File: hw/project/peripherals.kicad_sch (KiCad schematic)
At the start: 72 parts, among them J1 Battery, J10 I2C, J11 Voltage Monitor, J12 Misc, J2 Phases, J3 FTSH-107-01-L-DV-K-A, J4 Throttle, J5 Hall, J6 Serial, J7 SPI, J8 2.54 Comm, J9 CAN, SW3 USER, U3 ATA6561-GAQW-N

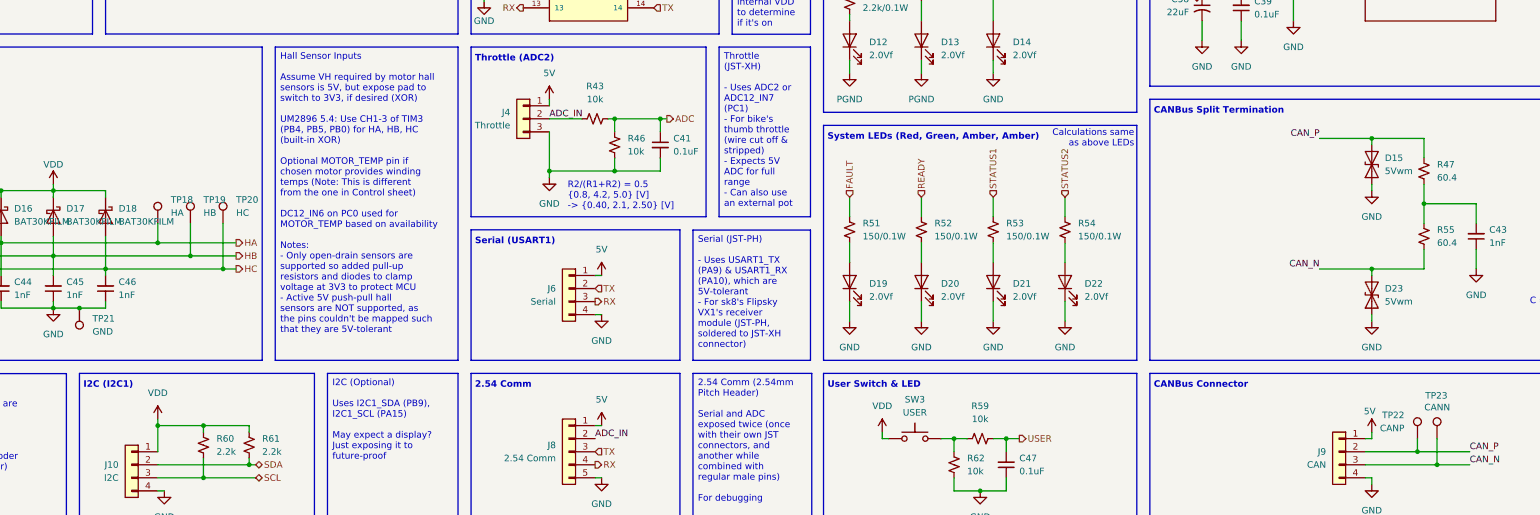
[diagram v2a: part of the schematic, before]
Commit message: Place next tier of components after critical ones
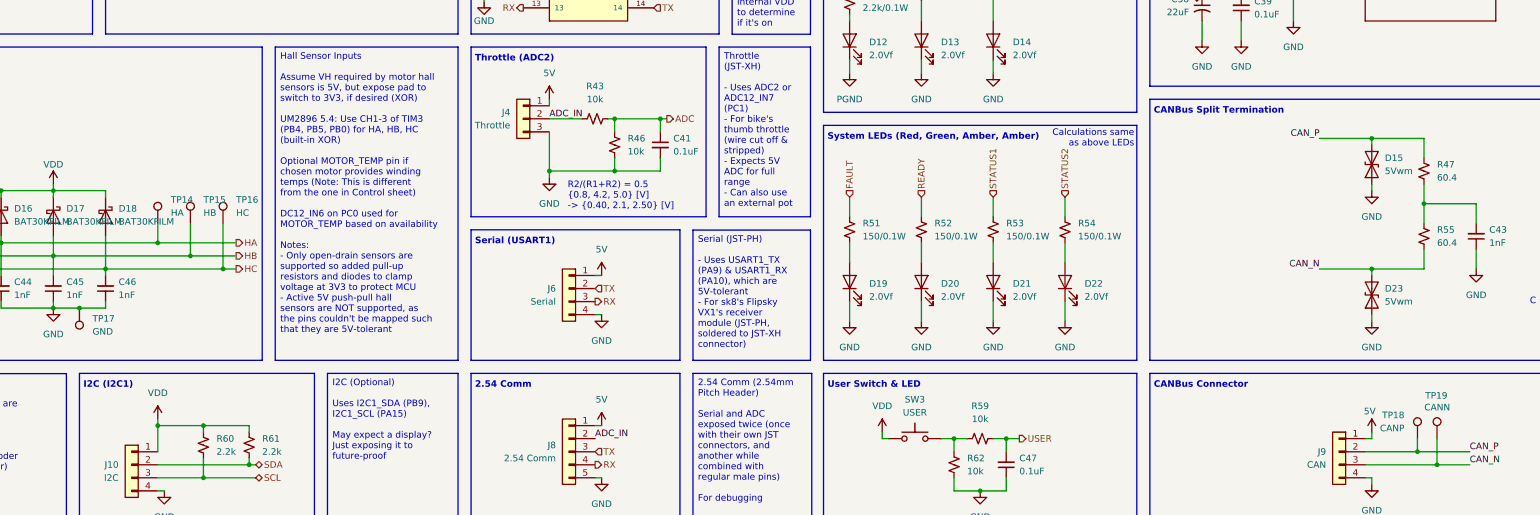
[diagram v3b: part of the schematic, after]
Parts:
- D12, D13, D14, D19, D20, D21, D22: footprint LED_SMD:LED_0603_1608Metric_Pad1.05x0.95mm_HandSolder -> LED_SMD:LED_0603_1608Metric
- R38, R40, R41, R51, R52, R53, R54: footprint Resistor_SMD:R_0603_1608Metric_Pad0.98x0.95mm_HandSolder -> Resistor_SMD:R_0603_1608Metric
- renumbered TP18 to TP14, TP19 to TP15, TP20 to TP16, TP21 to TP17, TP22 to TP18, TP23 to TP19
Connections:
- net GND: now also D13.1 (K)
- net PGND: no longer D13.1 (K)

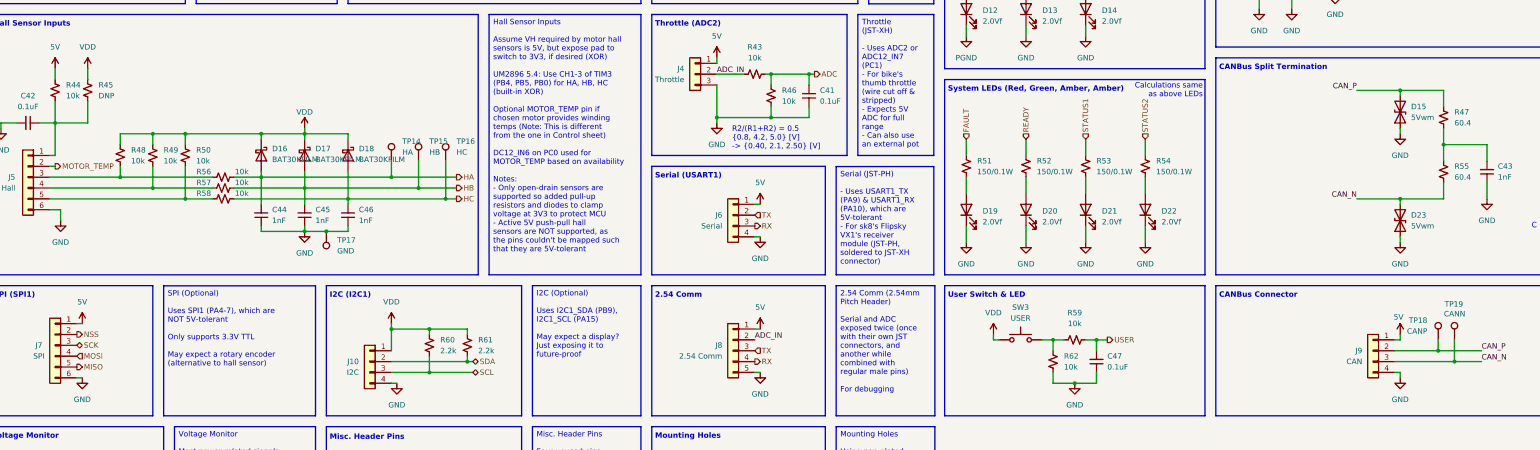
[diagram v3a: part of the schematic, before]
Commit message: Finish laying out all clusters
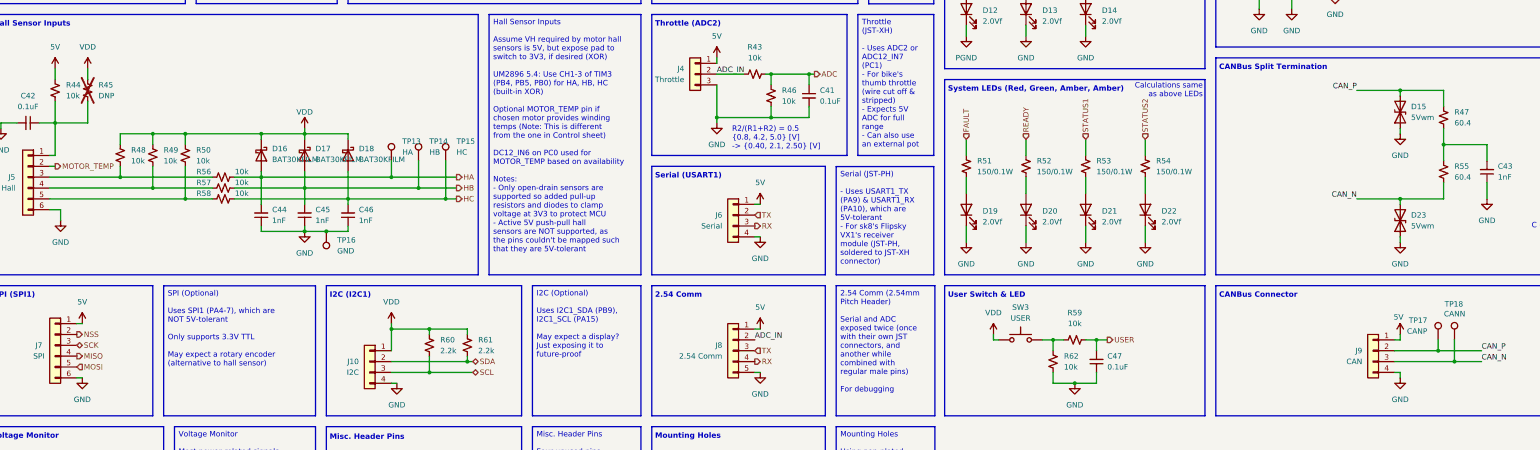
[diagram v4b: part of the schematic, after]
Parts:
- R45: now not fitted
- renumbered TP14 to TP13, TP15 to TP14, TP16 to TP15, TP17 to TP16, TP18 to TP17, TP19 to TP18
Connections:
- net MISO: now also J7.4 (Pin_4); no longer J7.5 (Pin_5)
- net MOSI: now also J7.5 (Pin_5); no longer J7.4 (Pin_4)
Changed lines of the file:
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@@
 	(hierarchical_label "MISO"
 		(shape output)
-		(at 35.56 133.35 0)
+		(at 35.56 130.81 0)
 		(effects
 			(font
@@
 	(hierarchical_label "MOSI"
 		(shape input)
-		(at 35.56 130.81 0)
+		(at 35.56 133.35 0)
 		(effects
 			(font
@@
 		(dnp no)
 		(fields_autoplaced yes)
-		(property "Reference" "#PWR0105"
+		(property "Reference" "#PWR070"
 			(at 257.81 62.23 0)
 			(hide yes)
@@
 			(project "esc"
 				(path "/86a17c4d-db96-42a1-af84-d43fe593f4e6/84ea8536-46c8-4cae-8743-a6718dee2882"
-					(reference "#PWR0105")
+					(reference "#PWR070")
 					(unit 1)
 				)
@@
 		(on_board yes)
 		(in_pos_files yes)
-		(dnp no)
+		(dnp yes)
 		(fields_autoplaced yes)
 		(property "Reference" "R45"
@@
 		(dnp no)
 		(fields_autoplaced yes)
-		(property "Reference" "TP14"
+		(property "Reference" "TP13"
 			(at 111.76 80.5179 0)
 			(show_name no)
@@
 			(project "esc"
 				(path "/86a17c4d-db96-42a1-af84-d43fe593f4e6/84ea8536-46c8-4cae-8743-a6718dee2882"
-					(reference "TP14")
+					(reference "TP13")
 					(unit 1)
 				)
@@
 		(dnp no)
 		(fields_autoplaced yes)
-		(property "Reference" "TP16"
+		(property "Reference" "TP15"
 			(at 124.46 80.5179 0)
 			(show_name no)
@@
 			(project "esc"
 				(path "/86a17c4d-db96-42a1-af84-d43fe593f4e6/84ea8536-46c8-4cae-8743-a6718dee2882"
-					(reference "TP16")
+					(reference "TP15")
 					(unit 1)
 				)
@@
 		(in_pos_files yes)
 		(dnp no)
-		(property "Reference" "TP19"
+		(property "Reference" "TP18"
 			(at 360.172 118.618 0)
 			(show_name no)
@@
 			(project "esc"
 				(path "/86a17c4d-db96-42a1-af84-d43fe593f4e6/84ea8536-46c8-4cae-8743-a6718dee2882"
-					(reference "TP19")
+					(reference "TP18")
 					(unit 1)
 				)
@@
 		(dnp no)
 		(fields_autoplaced yes)
-		(property "Reference" "TP18"
+		(property "Reference" "TP17"
 			(at 351.79 122.4279 0)
 			(show_name no)
@@
 			(project "esc"
 				(path "/86a17c4d-db96-42a1-af84-d43fe593f4e6/84ea8536-46c8-4cae-8743-a6718dee2882"
-					(reference "TP18")
+					(reference "TP17")
 					(unit 1)
 				)
@@
 		(dnp no)
 		(fields_autoplaced yes)
-		(property "Reference" "TP17"
+		(property "Reference" "TP16"
 			(at 96.52 103.6319 0)
 			(show_name no)
@@
 			(project "esc"
 				(path "/86a17c4d-db96-42a1-af84-d43fe593f4e6/84ea8536-46c8-4cae-8743-a6718dee2882"
-					(reference "TP17")
+					(reference "TP16")
 					(unit 1)
 				)
@@
 		(dnp no)
 		(fields_autoplaced yes)
-		(property "Reference" "TP15"
+		(property "Reference" "TP14"
 			(at 118.11 80.5179 0)
 			(show_name no)
@@
 			(project "esc"
 				(path "/86a17c4d-db96-42a1-af84-d43fe593f4e6/84ea8536-46c8-4cae-8743-a6718dee2882"
-					(reference "TP15")
+					(reference "TP14")
 					(unit 1)
 				)

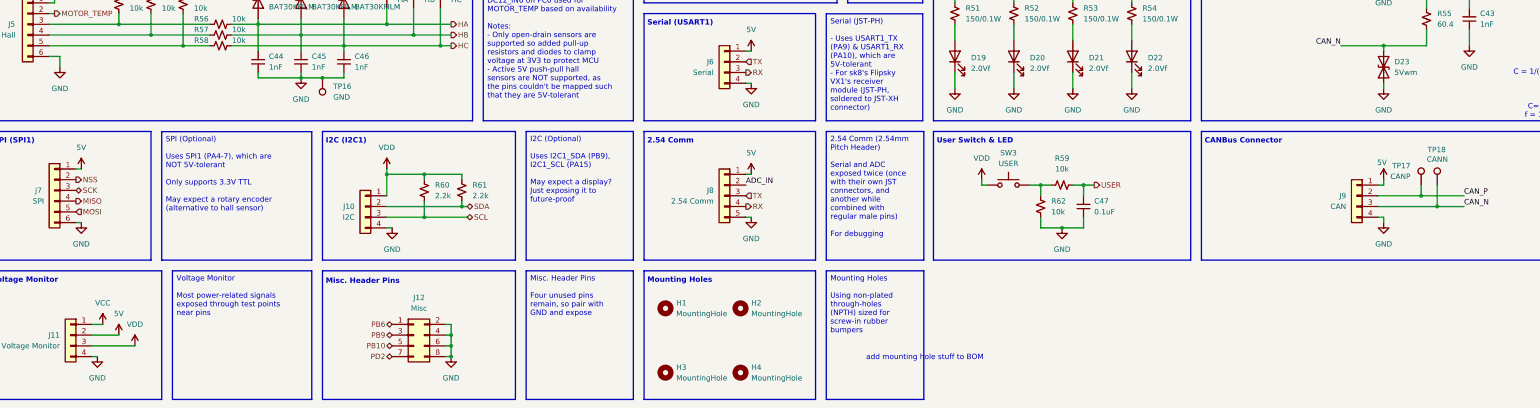
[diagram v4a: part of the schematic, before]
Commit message: Finish most of the layout, just the power stuff next!
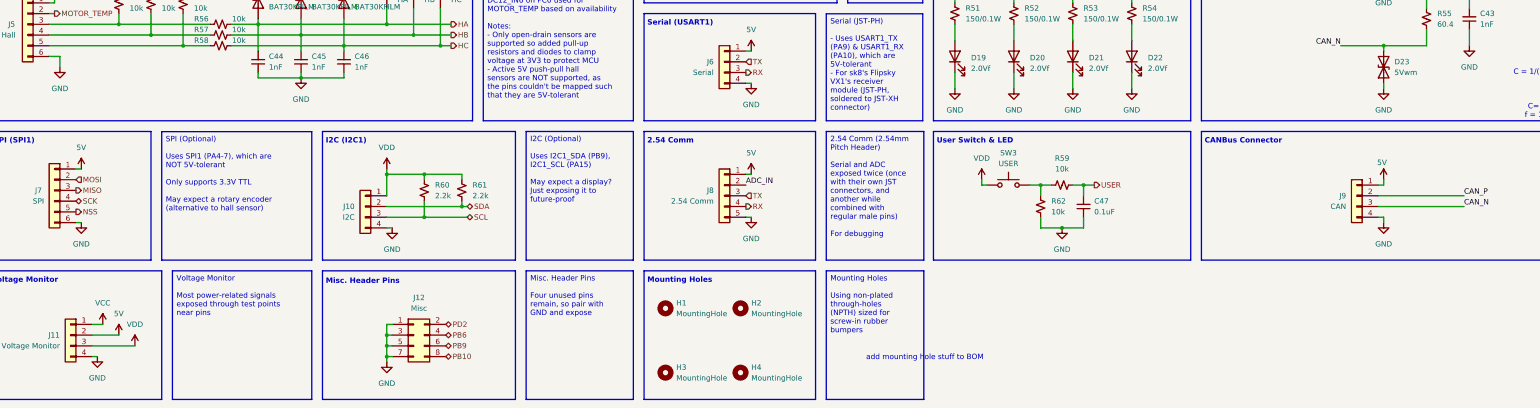
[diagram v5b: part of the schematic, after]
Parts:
- removed TP16: GND, TestPoint:TestPoint_Pad_1.0x1.0mm, symbol Connector:TestPoint
- removed TP17: CANP, TestPoint:TestPoint_Pad_D1.0mm, symbol Connector:TestPoint
- removed TP18: CANN, TestPoint:TestPoint_Pad_D1.0mm, symbol Connector:TestPoint
- J8: footprint Connector_PinSocket_2.54mm:PinSocket_1x05_P2.54mm_Vertical -> Connector_PinHeader_2.54mm:PinHeader_1x05_P2.54mm_Vertical
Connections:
- net GND: now also J12.1 (Pin_1), J12.3 (Pin_3), J12.5 (Pin_5), J12.7 (Pin_7); no longer J12.2 (Pin_2), J12.4 (Pin_4), J12.6 (Pin_6), J12.8 (Pin_8)
- net MISO: now also J7.3 (Pin_3); no longer J7.4 (Pin_4)
- net MOSI: now also J7.2 (Pin_2); no longer J7.5 (Pin_5)
- net NSS: now also J7.5 (Pin_5); no longer J7.2 (Pin_2)
- net PB10: now also J12.8 (Pin_8); no longer J12.5 (Pin_5)
- net PB6: now also J12.4 (Pin_4); no longer J12.1 (Pin_1)
- net PB9: now also J12.6 (Pin_6); no longer J12.3 (Pin_3)
- net PD2: now also J12.2 (Pin_2); no longer J12.7 (Pin_7)
- net SCK: now also J7.4 (Pin_4); no longer J7.3 (Pin_3)

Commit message: Rotate some parts in drive section
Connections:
- net PGND: now also J1.1, J1.2; no longer J1.3, J1.4
- net U: now also J2.3, J2.A3; no longer J2.1, J2.A1
- net VM_IN: now also J1.3, J1.4; no longer J1.1, J1.2
- net W: now also J2.1, J2.A1; no longer J2.3, J2.A3

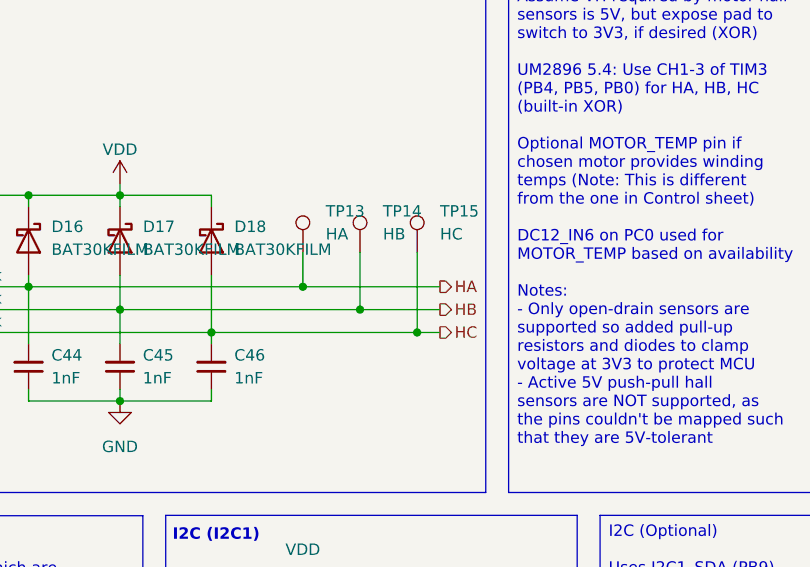
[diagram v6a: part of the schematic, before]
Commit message: Label JST connectors
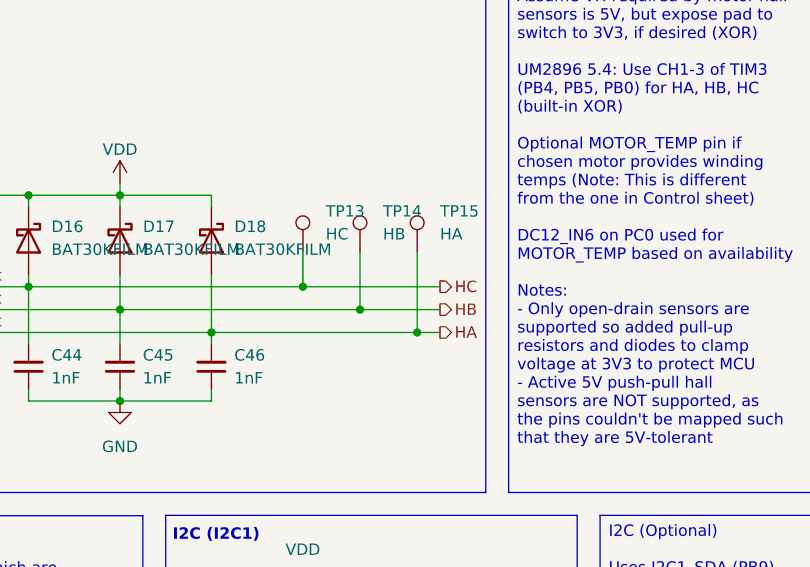
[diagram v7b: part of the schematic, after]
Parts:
- TP13: value HA -> HC
- TP15: value HC -> HA
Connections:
- net HA: now also C46.2, D18.2 (A), R58.2, TP15.1; no longer C44.2, D16.2 (A), R56.2, TP13.1
- net HC: now also C44.2, D16.2 (A), R56.2, TP13.1; no longer C46.2, D18.2 (A), R58.2, TP15.1
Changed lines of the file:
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@@
 	(hierarchical_label "HC"
 		(shape output)
-		(at 124.46 93.98 0)
+		(at 124.46 88.9 0)
 		(effects
 			(font
@@
 	(hierarchical_label "HA"
 		(shape output)
-		(at 124.46 88.9 0)
+		(at 124.46 93.98 0)
 		(effects
 			(font
@@
 			)
 		)
-		(property "Value" "HA"
+		(property "Value" "HC"
 			(at 111.76 83.0579 0)
 			(show_name no)
@@
 			)
 		)
-		(property "Value" "HC"
+		(property "Value" "HA"
 			(at 124.46 83.0579 0)
 			(show_name no)

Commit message: Label everythangg
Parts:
- added TP16: CANL, TestPoint:TestPoint_Pad_D1.0mm, symbol Connector:TestPoint
- added TP17: CANH, TestPoint:TestPoint_Pad_D1.0mm, symbol Connector:TestPoint
- TP13: value HC -> HA
- TP15: value HA -> HC
- renumbered J12 to J11, J11 to J12, J8 to J7, J7 to J8, R56 to R51, R51 to R52, R52 to R53, R53 to R54, R54 to R55, R55 to R56
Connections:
- net 5V: now also J12.3 (Pin_3), J4.3 (Pin_3), J6.4 (Pin_4), J7.5 (Pin_5), J8.6 (Pin_6), J9.4 (Pin_4); no longer J12.2 (Pin_2), J4.1 (Pin_1), J6.1 (Pin_1), J7.1 (Pin_1), J8.1 (Pin_1), J9.1 (Pin_1)
- net CAN_N: now also TP16.1
- net CAN_P: now also TP17.1
- net GND: now also J10.1 (Pin_1), J12.1 (Pin_1), J4.1 (Pin_1), J5.1 (Pin_1), J6.1 (Pin_1), J7.1 (Pin_1), J8.1 (Pin_1), J9.1 (Pin_1); no longer J10.4 (Pin_4), J12.4 (Pin_4), J4.3 (Pin_3), J5.6 (Pin_6), J6.4 (Pin_4), J7.5 (Pin_5), J8.6 (Pin_6), J9.4 (Pin_4)
- net HA: now also C44.2, D16.2 (A), R51.2, TP13.1; no longer C46.2, D18.2 (A), R58.2, TP15.1
- net HC: now also C46.2, D18.2 (A), R58.2, TP15.1; no longer C44.2, D16.2 (A), R51.2, TP13.1
- net SCL: now also R61.1; no longer R60.1
- net SDA: now also R60.1; no longer R61.1
- net VCC: now also J12.4 (Pin_4); no longer J12.1 (Pin_1)
- net VDD: now also J10.4 (Pin_4), J12.2 (Pin_2); no longer J10.1 (Pin_1), J12.3 (Pin_3)
- net at C42.1, R44.2, R45.2: now also J5.6 (Pin_6); no longer J5.1 (Pin_1)
- net at R50.2, R58.1: now also J5.3 (Pin_3); no longer J5.5 (Pin_5)
- net at R48.2, R51.1: now also J5.5 (Pin_5); no longer J5.3 (Pin_3)
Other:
- moved on the sheet: C44, C45, C46, D16, D17, D18, J10, J12, J4, J5, J6, J7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
